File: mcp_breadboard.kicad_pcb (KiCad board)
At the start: 2 copper layers, 53.3 x 35.6 mm, 30 parts, among them J1 VDD, J2 VDD, J3 GPIO, J4 UART/SPI, J5 USB_B_Micro, SW1 RST, SW2 SW_DIP_x04, SW3 VDD_SEL, U1 MCP2221AxSL, U2 MCP1826S

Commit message: Final minor board tweaks
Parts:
- moved R3 10.5 mm to (44.8, 44.2), turned to 180 degrees
- moved C2 1.50 mm to (55.2, 44.1)
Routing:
- net Net-(R3-Pad1): track 22.3 -> 23.6 mm
- net unconnected-(J5-Pad6): track 13.8 -> 12.6 mm
- net Net-(C2-Pad1): track 2.74 -> 2.04 mm
- net G1: vias 2 -> 3
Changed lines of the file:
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@@
   )
   (footprint "Resistor_SMD:R_0603_1608Metric" (layer "F.Cu")
-    (at 55.25 44.15)
+    (at 44.75 44.25 180)
     (descr "Resistor SMD 0603 (1608 Metric), square (rectangular) end terminal, IPC_7351 nominal, (Body size source: IPC-SM-782 page 72, https://www.pcb-3d.com/wordpress/wp-content/uploads/ipc-sm-782a_amendment_1_and_2.pdf), generated with kicad-footprint-generator")
     (tags "resistor")
@@
     (property "Sheetname" "")
     (attr smd)
-    (fp_text reference "R3" (at 2.35 0) (layer "F.SilkS")
+    (fp_text reference "R3" (at -0.05 -1.4) (layer "F.SilkS")
       (effects (font (size 1 1) (thickness 0.15)))
     )
@@
     (fp_line (start 0.8 -0.4125) (end 0.8 0.4125) (layer "F.Fab") (width 0.1))
     (fp_line (start 0.8 0.4125) (end -0.8 0.4125) (layer "F.Fab") (width 0.1))
-    (pad "1" smd roundrect (at -0.825 0) (size 0.8 0.95) (layers "F.Cu" "F.Paste" "F.Mask") (roundrect_rratio 0.25)
+    (pad "1" smd roundrect (at -0.825 0 180) (size 0.8 0.95) (layers "F.Cu" "F.Paste" "F.Mask") (roundrect_rratio 0.25)
       (net 19 "Net-(R3-Pad1)") (pintype "passive"))
-    (pad "2" smd roundrect (at 0.825 0) (size 0.8 0.95) (layers "F.Cu" "F.Paste" "F.Mask") (roundrect_rratio 0.25)
+    (pad "2" smd roundrect (at 0.825 0 180) (size 0.8 0.95) (layers "F.Cu" "F.Paste" "F.Mask") (roundrect_rratio 0.25)
       (net 4 "VDD") (pintype "passive"))
     (model "${KICAD6_3DMODEL_DIR}/Resistor_SMD.3dshapes/R_0603_1608Metric.wrl"
@@
     (property "Sheetname" "")
     (attr smd)
-    (fp_text reference "C1" (at -0.025 -1.3) (layer "F.SilkS")
+    (fp_text reference "C1" (at 0 -1.4) (layer "F.SilkS")
       (effects (font (size 1 1) (thickness 0.15)))
     )
@@
   )
   (footprint "Capacitor_SMD:C_0603_1608Metric" (layer "F.Cu")
-    (at 55.25 42.65)
+    (at 55.25 44.15)
     (descr "Capacitor SMD 0603 (1608 Metric), square (rectangular) end terminal, IPC_7351 nominal, (Body size source: IPC-SM-782 page 76, https://www.pcb-3d.com/wordpress/wp-content/uploads/ipc-sm-782a_amendment_1_and_2.pdf), generated with kicad-footprint-generator")
     (tags "capacitor")
@@
   (segment (start 48.7 33.44) (end 48.7 32.4625) (width 0.25) (layer "F.Cu") (net 2))
   (segment (start 50.331 34.012351) (end 50.331 34.5895) (width 0.25) (layer "F.Cu") (net 2))
-  (segment (start 56.8 42.65) (end 56.025 42.65) (width 0.25) (layer "F.Cu") (net 2))
   (segment (start 53.64 40.44) (end 53.7 40.5) (width 0.25) (layer "F.Cu") (net 2))
   (segment (start 57 31.3125) (end 57 32.077) (width 0.25) (layer "F.Cu") (net 2))
   (segment (start 43.2 40.45) (end 43.975 40.45) (width 0.25) (layer "F.Cu") (net 2))
+  (segment (start 56.8 44.15) (end 56.025 44.15) (width 0.25) (layer "F.Cu") (net 2))
   (segment (start 52.475 40.44) (end 53.64 40.44) (width 0.25) (layer "F.Cu") (net 2))
   (via (at 67.55 34.55) (size 0.6) (drill 0.3) (layers "F.Cu" "B.Cu") (free) (net 2))
@@
   (via (at 62.4 29.45) (size 0.6) (drill 0.3) (layers "F.Cu" "B.Cu") (free) (net 2))
   (via (at 63.51 35.14) (size 0.6) (drill 0.3) (layers "F.Cu" "B.Cu") (free) (net 2))
-  (via (at 56.8 42.65) (size 0.6) (drill 0.3) (layers "F.Cu" "B.Cu") (net 2))
+  (via (at 56.8 44.15) (size 0.6) (drill 0.3) (layers "F.Cu" "B.Cu") (net 2))
   (via (at 43.2 40.45) (size 0.6) (drill 0.3) (layers "F.Cu" "B.Cu") (net 2))
   (via (at 63.55 37.75) (size 0.6) (drill 0.3) (layers "F.Cu" "B.Cu") (free) (net 2))
@@
   (segment (start 66.54 41.16) (end 64.32 43.38) (width 0.4) (layer "B.Cu") (net 3))
   (segment (start 47.525 40.44) (end 45.51 40.44) (width 0.25) (layer "F.Cu") (net 4))
-  (segment (start 54.475 42.775) (end 54.475 42.65) (width 0.25) (layer "F.Cu") (net 5))
-  (segment (start 53 44.25) (end 54.475 42.775) (width 0.25) (layer "F.Cu") (net 5))
-  (segment (start 52.475 44.25) (end 53 44.25) (width 0.25) (layer "F.Cu") (net 5))
+  (segment (start 53.7 44.25) (end 53.8 44.15) (width 0.25) (layer "F.Cu") (net 5))
+  (segment (start 53.8 44.15) (end 54.475 44.15) (width 0.25) (layer "F.Cu") (net 5))
+  (segment (start 52.475 44.25) (end 53.7 44.25) (width 0.25) (layer "F.Cu") (net 5))
   (segment (start 41.5 33.75) (end 41.5 33.1875) (width 0.25) (layer "F.Cu") (net 6))
   (segment (start 40.81 35.695) (end 40.81 34.44) (width 0.25) (layer "F.Cu") (net 6))
@@
   (segment (start 57 34.675) (end 57 33.1355) (width 0.25) (layer "F.Cu") (net 10))
   (segment (start 46.5 54.5) (end 45.92 55.08) (width 0.25) (layer "F.Cu") (net 11))
+  (segment (start 44.75 43.2) (end 44.75 46.25) (width 0.25) (layer "F.Cu") (net 11))
   (segment (start 44.75 50.17) (end 46.5 51.92) (width 0.25) (layer "F.Cu") (net 11))
   (segment (start 43.25 46.675) (end 44.75 46.675) (width 0.25) (layer "F.Cu") (net 11))
-  (segment (start 44.75 43.2) (end 44.75 50.17) (width 0.25) (layer "F.Cu") (net 11))
   (segment (start 47.525 41.71) (end 46.24 41.71) (width 0.25) (layer "F.Cu") (net 11))
   (segment (start 46.5 51.92) (end 46.5 54.5) (width 0.25) (layer "F.Cu") (net 11))
+  (segment (start 44.75 46.25) (end 44.75 50.17) (width 0.25) (layer "F.Cu") (net 11))
   (segment (start 45.92 55.08) (end 44.92 55.08) (width 0.25) (layer "F.Cu") (net 11))
   (segment (start 46.24 41.71) (end 44.75 43.2) (width 0.25) (layer "F.Cu") (net 11))
   (segment (start 47 51.67) (end 47 57) (width 0.25) (layer "F.Cu") (net 12))
-  (segment (start 45.72 42.98) (end 47.525 42.98) (width 0.25) (layer "F.Cu") (net 12))
   (segment (start 43.93503 47.475) (end 43.25 47.475) (width 0.25) (layer "F.Cu") (net 12))
   (segment (start 47 57) (end 46.38 57.62) (width 0.25) (layer "F.Cu") (net 12))
-  (segment (start 45.5 47.5) (end 45.5 43.2) (width 0.25) (layer "F.Cu") (net 12))
-  (segment (start 45.5 43.2) (end 45.72 42.98) (width 0.25) (layer "F.Cu") (net 12))
+  (segment (start 46.27 42.98) (end 47.525 42.98) (width 0.25) (layer "F.Cu") (net 12))
   (segment (start 45.5 50.17) (end 47 51.67) (width 0.25) (layer "F.Cu") (net 12))
   (segment (start 45.5 47.5) (end 45.5 50.17) (width 0.25) (layer "F.Cu") (net 12))
   (segment (start 43.953019 47.492989) (end 43.93503 47.475) (width 0.25) (layer "F.Cu") (net 12))
   (segment (start 46.38 57.62) (end 44.92 57.62) (width 0.25) (layer "F.Cu") (net 12))
+  (via (at 46.27 42.98) (size 0.6) (drill 0.3) (layers "F.Cu" "B.Cu") (net 12))
   (via (at 45.5 47.5) (size 0.6) (drill 0.3) (layers "F.Cu" "B.Cu") (net 12))
   (via (at 43.953019 47.492989) (size 0.6) (drill 0.3) (layers "F.Cu" "B.Cu") (net 12))
+  (segment (start 45.77 42.98) (end 45.5 43.25) (width 0.25) (layer "B.Cu") (net 12))
   (segment (start 45.5 47.5) (end 45.492989 47.492989) (width 0.25) (layer "B.Cu") (net 12))
   (segment (start 45.492989 47.492989) (end 43.953019 47.492989) (width 0.25) (layer "B.Cu") (net 12))
+  (segment (start 46.27 42.98) (end 45.77 42.98) (width 0.25) (layer "B.Cu") (net 12))
+  (segment (start 45.5 43.25) (end 45.5 47.5) (width 0.25) (layer "B.Cu") (net 12))
   (segment (start 47.5 59.5) (end 46.84 60.16) (width 0.25) (layer "F.Cu") (net 13))
   (segment (start 47.5 51.42) (end 47.5 59.5) (width 0.25) (layer "F.Cu") (net 13))
@@
   (segment (start 55.25 46) (end 54.9 45.65) (width 0.25) (layer "F.Cu") (net 18))
   (segment (start 53.8 45.65) (end 53.67 45.52) (width 0.25) (layer "F.Cu") (net 18))
-  (segment (start 53.675 44.9) (end 54.425 44.15) (width 0.25) (layer "F.Cu") (net 19))
   (segment (start 67.975 47.25) (end 60.025 47.25) (width 0.25) (layer "F.Cu") (net 19))
-  (segment (start 55.1 44.15) (end 54.425 44.15) (width 0.25) (layer "F.Cu") (net 19))
   (segment (start 50.95 44.9) (end 53.675 44.9) (width 0.25) (layer "F.Cu") (net 19))
-  (segment (start 60.025 47.25) (end 58.75 47.25) (width 0.25) (layer "F.Cu") (net 19))
+  (segment (start 60.025 47.25) (end 58.95 47.25) (width 0.25) (layer "F.Cu") (net 19))
   (segment (start 50.3 44.25) (end 50.95 44.9) (width 0.25) (layer "F.Cu") (net 19))
+  (segment (start 53.675 44.9) (end 55.25 44.9) (width 0.25) (layer "F.Cu") (net 19))
   (segment (start 47.525 44.25) (end 50.3 44.25) (width 0.25) (layer "F.Cu") (net 19))
-  (via (at 58.75 47.25) (size 0.6) (drill 0.3) (layers "F.Cu" "B.Cu") (net 19))
-  (via (at 55.1 44.15) (size 0.6) (drill 0.3) (layers "F.Cu" "B.Cu") (net 19))
-  (segment (start 58.75 47.25) (end 55.65 44.15) (width 0.25) (layer "B.Cu") (net 19))
-  (segment (start 55.65 44.15) (end 55.1 44.15) (width 0.25) (layer "B.Cu") (net 19))
+  (segment (start 47.525 44.25) (end 45.575 44.25) (width 0.25) (layer "F.Cu") (net 19))
+  (via (at 58.95 47.25) (size 0.6) (drill 0.3) (layers "F.Cu" "B.Cu") (net 19))
+  (via (at 55.25 44.9) (size 0.6) (drill 0.3) (layers "F.Cu" "B.Cu") (net 19))
+  (segment (start 58.95 47.25) (end 57.6 47.25) (width 0.25) (layer "B.Cu") (net 19))
+  (segment (start 57.6 47.25) (end 55.25 44.9) (width 0.25) (layer "B.Cu") (net 19))
   (segment (start 50.85 36.015) (end 50.85 35.326351) (width 0.2) (layer "F.Cu") (net 20))
   (segment (start 50.85 35.326351) (end 50.831 35.307351) (width 0.2) (layer "F.Cu") (net 20))
@@
   (segment (start 50.25 41.75) (end 50.25 36.44) (width 0.2) (layer "B.Cu") (net 21))
   (segment (start 50.25 36.44) (end 49.825 36.015) (width 0.2) (layer "B.Cu") (net 21))
-  (segment (start 52.5 30.1625) (end 52.9 29.7625) (width 0.25) (layer "F.Cu") (net 23))
   (segment (start 47.1 29.7625) (end 53.5 29.7625) (width 0.25) (layer "F.Cu") (net 23))
-  (segment (start 47.5 30.1625) (end 47.1 29.7625) (width 0.25) (layer "F.Cu") (net 23))
   (segment (start 53.5 31.4625) (end 53.5 29.7625) (width 0.25) (layer "B.Cu") (net 23))
   (segment (start 47.5 32.4625) (end 46.5 31.4625) (width 0.25) (layer "B.Cu") (net 23))

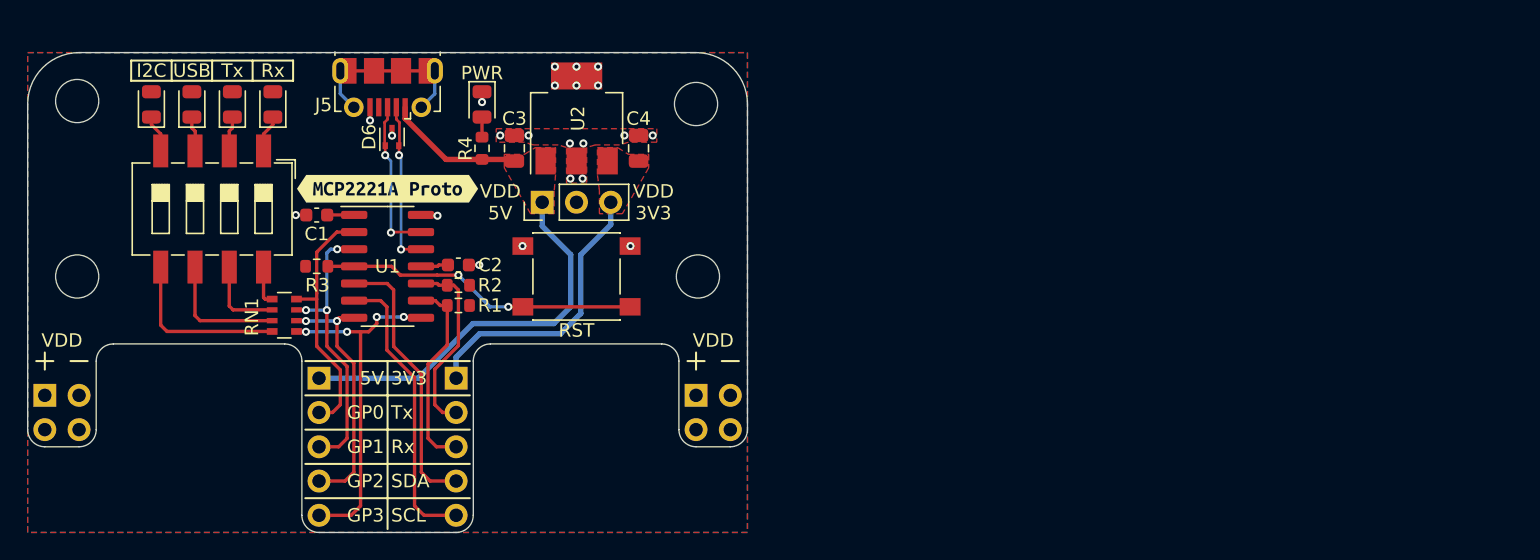
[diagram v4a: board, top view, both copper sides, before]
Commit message: Fix board outline for breadboard meshing.
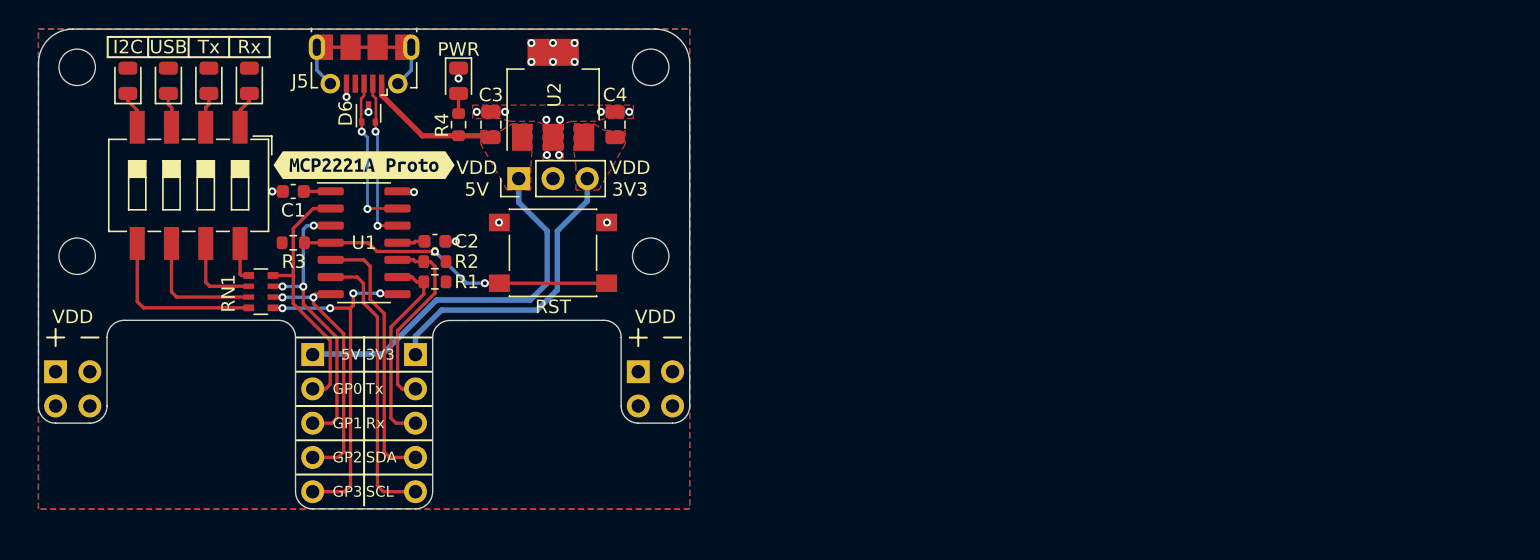
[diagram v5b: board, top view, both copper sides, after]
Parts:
- H1, H2, H3, H4: footprint MountingHole:MountingHole_3.2mm_M3_ISO7380 -> MountingHole:MountingHole_2.7mm_M2.5_ISO7380
- moved J2 4.62 mm to (68.6, 52.1)
- moved H3 4.32 mm to (69.5, 29.5)
- moved H4 3.81 mm to (69.5, 43.5)
- moved J4 3.48 mm to (52.1, 50.8)
- moved H2 2.50 mm to (27.0, 29.5)
- moved C1 2.47 mm to (43.0, 38.7)
- moved C2 2.47 mm to (53.5, 42.4)
- moved C3 2.47 mm to (57.7, 33.8)
- moved D1 2.47 mm to (39.8, 30.5)
- moved D2 2.47 mm to (36.8, 30.5)
- moved D3 2.47 mm to (33.8, 30.5)
- moved D5 2.47 mm to (55.3, 30.5)
- moved D6 2.47 mm to (48.6, 32.9)
- moved J5 2.47 mm to (48.3, 29.2)
- moved R1 2.47 mm to (53.5, 45.4)
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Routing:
- net +5V: track 39.7 -> 38.4 mm
- net Rx: track 20.3 -> 19.1 mm
- net +3V3: track 21.3 -> 22.4 mm
- net SCL: track 14.0 -> 14.6 mm
- net Tx: track 21.6 -> 21.1 mm
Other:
- board size 53.3 x 35.6 mm -> 48.3 x 35.5 mm
